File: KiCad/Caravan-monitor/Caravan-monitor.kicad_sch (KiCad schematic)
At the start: 11 parts, among them IC2 STM32L011F4P6TR, J1 Conn_ARM_JTAG_SWD_20, J2 PJ-059A, SW1 SW_SPST

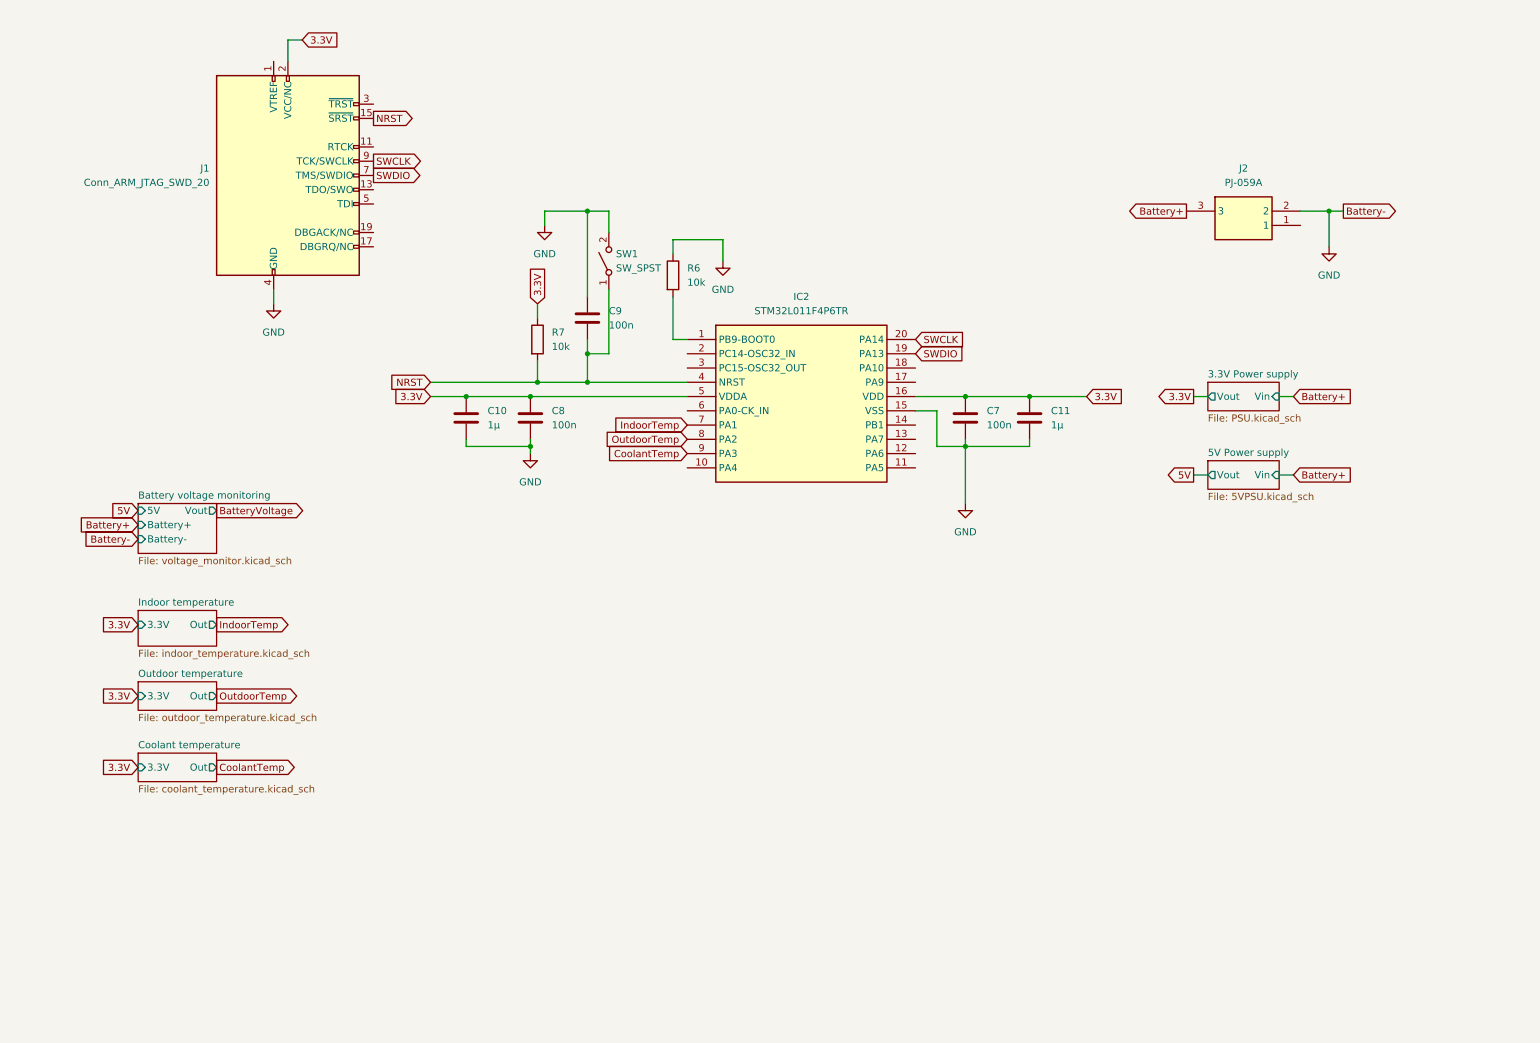
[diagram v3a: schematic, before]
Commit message: Display schematics
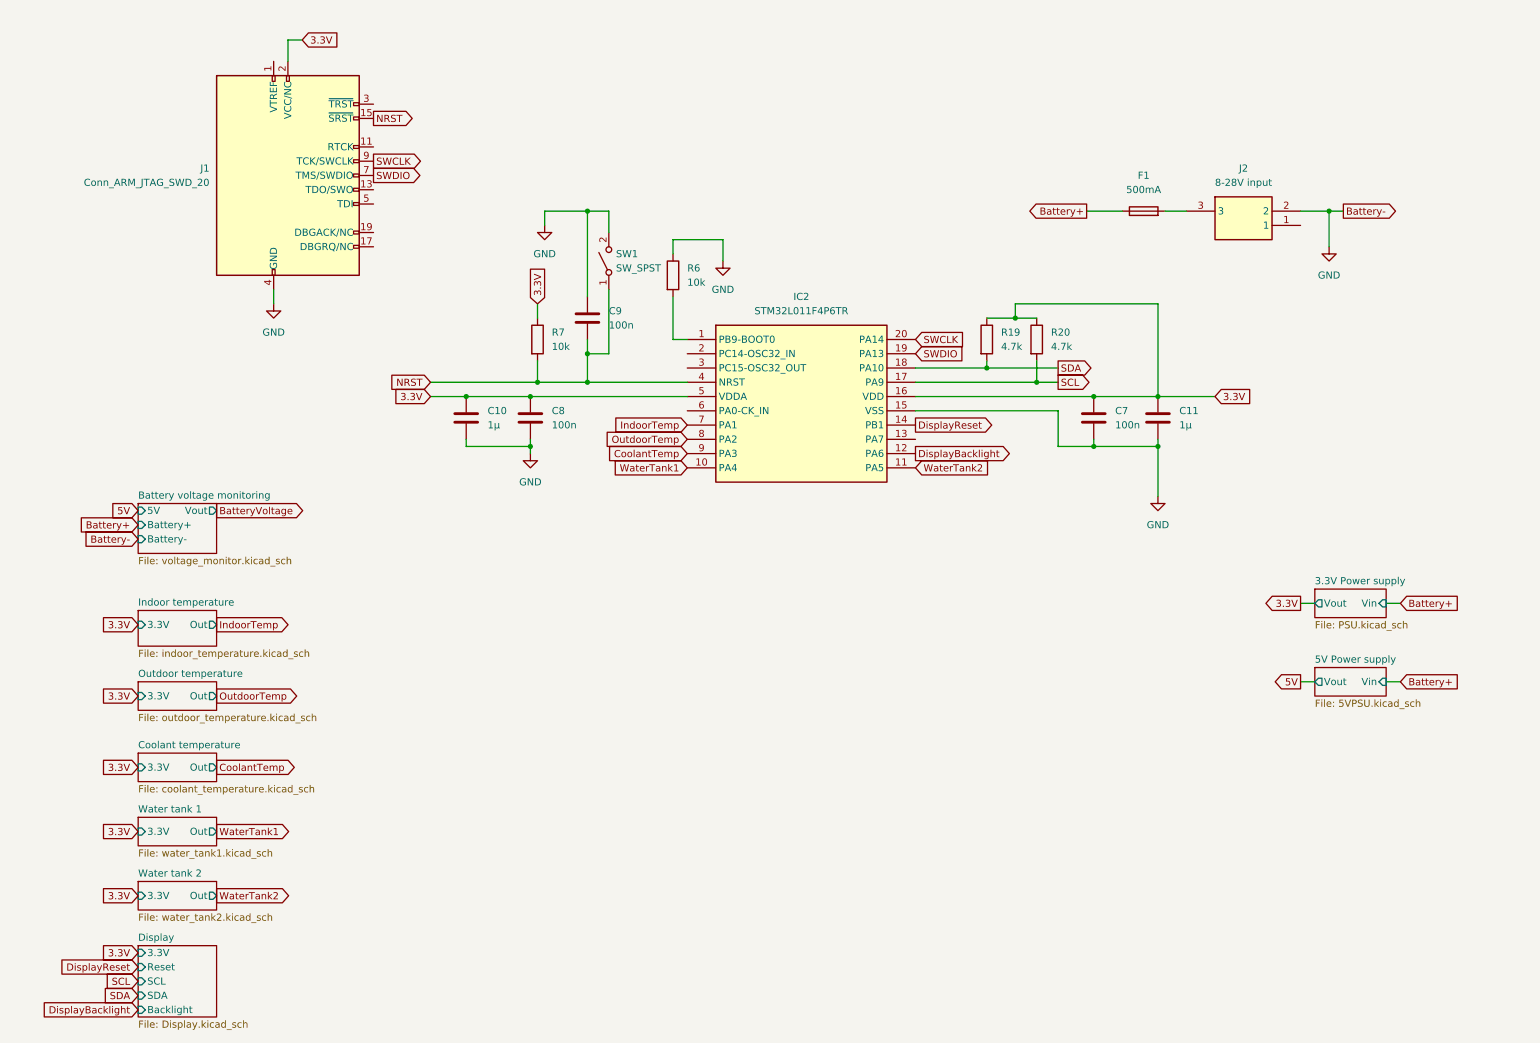
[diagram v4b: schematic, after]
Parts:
- added F1: 500mA, Fuse:Fuseholder_Clip-5x20mm_Littelfuse_111_Lateral_P18.80x5.00mm_D1.17mm_Horizontal, symbol Device:Fuse
- added R19, R20: 4.7k, Resistor_SMD:R_0805_2012Metric_Pad1.20x1.40mm_HandSolder, symbol Device:R
- J1: footprint Connector_IDC:IDC-Header_2x10_P2.54mm_Vertical -> Connector_IDC:IDC-Header_2x10_P2.54mm_Horizontal
- J2: value PJ-059A -> 8-28V input
- SW1: footprint (none) -> Button_Switch_SMD:SW_SPST_PTS645
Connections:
- net 3.3V: now also R19.1, R20.1
- net Battery+: now also F1.1; no longer J2.3
- net WaterTank1: now reaches IC2.10 (PA4)
- net WaterTank2: now reaches IC2.11 (PA5)
- net DisplayBacklight: now reaches IC2.12 (PA6)
- net DisplayReset: now reaches IC2.14 (PB1)
- net SCL: now reaches IC2.17 (PA9)
- net SCL: now also R20.2
- net SDA: now reaches IC2.18 (PA10)
- net SDA: now also R19.2
- new net: F1.2, J2.3
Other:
- added sheet Display (Display.kicad_sch)
- added sheet Water tank 1 (water_tank1.kicad_sch)
- added sheet Water tank 2 (water_tank2.kicad_sch)
- moved on the sheet: C11, C7

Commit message: Schematics done
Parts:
- removed IC2: STM32L011F4P6TR, SamacSys_Parts:SOP65P640X120-20N, symbol SamacSys_Parts:STM32L011F4P6TR
- added C25, C27, C28: 100n, Capacitor_SMD:C_0402_1005Metric_Pad0.74x0.62mm_HandSolder, symbol Device:C
- added C26: 1µ, Capacitor_SMD:C_0402_1005Metric_Pad0.74x0.62mm_HandSolder, symbol Device:C
- added C29, C30: 10p, Capacitor_SMD:C_0402_1005Metric_Pad0.74x0.62mm_HandSolder, symbol Device:C
- added D2: WT1_LED, LED_SMD:LED_0402_1005Metric_Pad0.77x0.64mm_HandSolder, symbol Device:LED
- added D3: WT2_LED, LED_SMD:LED_0402_1005Metric_Pad0.77x0.64mm_HandSolder, symbol Device:LED
- added FB1: 120R, Inductor_SMD:L_0402_1005Metric_Pad0.77x0.64mm_HandSolder, symbol Device:FerriteBead
- added J8: STM32 Pins, Connector_PinHeader_2.54mm:PinHeader_2x13_P2.54mm_Horizontal, symbol Connector_Generic:Conn_02x13_Counter_Clockwise
- added R23: 10k, Resistor_SMD:R_0402_1005Metric_Pad0.72x0.64mm_HandSolder, symbol Device:R
- added R25, R8: 1k, Resistor_SMD:R_0402_1005Metric_Pad0.72x0.64mm_HandSolder, symbol Device:R
- added SW2: SW_USER, Button_Switch_SMD:SW_SPST_PTS645, symbol Switch:SW_SPST
- added SW3: SW_DPDT_x2, Button_Switch_THT:SW_E-Switch_EG2219_DPDT_Angled, symbol Switch:SW_DPDT_x2
- added U2: STM32L010C6Tx, Package_QFP:LQFP-48_7x7mm_P0.5mm, symbol MCU_ST_STM32L0:STM32L010C6Tx
- added Y1: 16MHz, symbol Device:Crystal_GND24
- C10, C11, C7, C9: footprint Capacitor_SMD:C_0805_2012Metric_Pad1.18x1.45mm_HandSolder -> Capacitor_SMD:C_0402_1005Metric_Pad0.74x0.62mm_HandSolder
- C8: value 100n -> 10n; footprint Capacitor_SMD:C_0805_2012Metric_Pad1.18x1.45mm_HandSolder -> Capacitor_SMD:C_0402_1005Metric_Pad0.74x0.62mm_HandSolder
- R19, R20, R6, R7: footprint Resistor_SMD:R_0805_2012Metric_Pad1.20x1.40mm_HandSolder -> Resistor_SMD:R_0402_1005Metric_Pad0.72x0.64mm_HandSolder
- SW1: value SW_SPST -> SW_RESET
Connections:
- net BatteryVoltage: now also U2.46 (PB9)
- net CoolantTemp: now also U2.27 (PB14)
- net DisplayBacklight: now also U2.45 (PB8)
- net DisplayReset: now also U2.43 (PB7)
- net GND: now also C25.1, C26.2, C27.2, C28.2, C29.2, C30.2, J8.13 (Pin_13), R25.2, R8.2, SW2.1 (A), U2.23 (VSS), U2.35 (VSS), U2.47 (VSS), U2.8 (VSSA), Y1.2, Y1.4
- net IndoorTemp: now also U2.25 (PB12)
- net NRST: now also U2.7 (NRST)
- net OutdoorTemp: now also U2.26 (PB13)
- net SCL: now also R19.2, U2.30 (PA9); no longer R20.2
- net SDA: now also R20.2, U2.31 (PA10); no longer R19.2
- net SWCLK: now also U2.37 (PA14)
- net SWDIO: now also U2.34 (PA13)
- net WaterTank1: now also U2.28 (PB15)
- net WaterTank2: now also U2.21 (PB10)
- net BOOT0: now reaches R6.2
- net BOOT0: now also U2.44 (BOOT0)
- net 3.3V renamed +3.3V
- net +3.3V: now also C26.1, C27.1, C28.1, FB1.2, J8.26 (Pin_26), R23.1, U2.24 (VDD), U2.36 (VDD), U2.48 (VDD); no longer C10.1, C8.1
- net Battery+: no longer names the net of F1.1
- net Battery+: now also SW3.2 (B)
- new net: D2.2 (A), J8.1 (Pin_1), U2.10 (PA0)
- new net: J8.10 (Pin_10), U2.32 (PA11)
- new net: J8.11 (Pin_11), U2.33 (PA12)
- new net: J8.12 (Pin_12), U2.38 (PA15)
- new net: D3.2 (A), J8.2 (Pin_2), U2.11 (PA1)
- new net: J8.3 (Pin_3), U2.12 (PA2)
- new net: J8.4 (Pin_4), U2.13 (PA3)
- new net: J8.5 (Pin_5), U2.14 (PA4)
- new net: J8.6 (Pin_6), U2.15 (PA5)
- new net: J8.7 (Pin_7), U2.16 (PA6)
- new net: J8.8 (Pin_8), U2.17 (PA7)
- new net: J8.9 (Pin_9), U2.29 (PA8)
- new net: C25.2, R23.2, SW2.2 (B), U2.22 (PB11)
- new net: D3.1 (K), R8.1
- new net: D2.1 (K), R25.1
- new net +3.3VA: C10.1, C8.1, FB1.1, U2.9 (VDDA)
- new net +5V: J8.25 (Pin_25)
- new net +BATT: SW3.1 (A)
- new net OSC_IN: C30.1, U2.5 (PH0), Y1.1
- new net OSC_OUT: C29.1, U2.6 (PH1), Y1.3
- new net PB0: J8.20 (Pin_20), U2.18 (PB0)
- new net PB1: J8.19 (Pin_19), U2.19 (PB1)
- new net PB2: J8.18 (Pin_18), U2.20 (PB2)
- new net PB3: J8.17 (Pin_17), U2.39 (PB3)
- new net PB4: J8.16 (Pin_16), U2.40 (PB4)
- new net PB5: J8.15 (Pin_15), U2.41 (PB5)
- new net PB6: J8.14 (Pin_14), U2.42 (PB6)
- new net PC0: J8.24 (Pin_24), U2.1 (PC0)
- new net PC13: J8.23 (Pin_23), U2.2 (PC13)
- new net PC14: J8.22 (Pin_22), U2.3 (PC14)
- new net PC15: J8.21 (Pin_21), U2.4 (PC15)
- no-connect marks 0 -> 9
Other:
- note added: "Connector for the rest of the pins if more sensors are wanted"
- note added: "Power supply"
- note added: "ST-Link connector"
- moved on the sheet: C10, C11, C7, C8, F1, J1, J2, R19, R20, R7

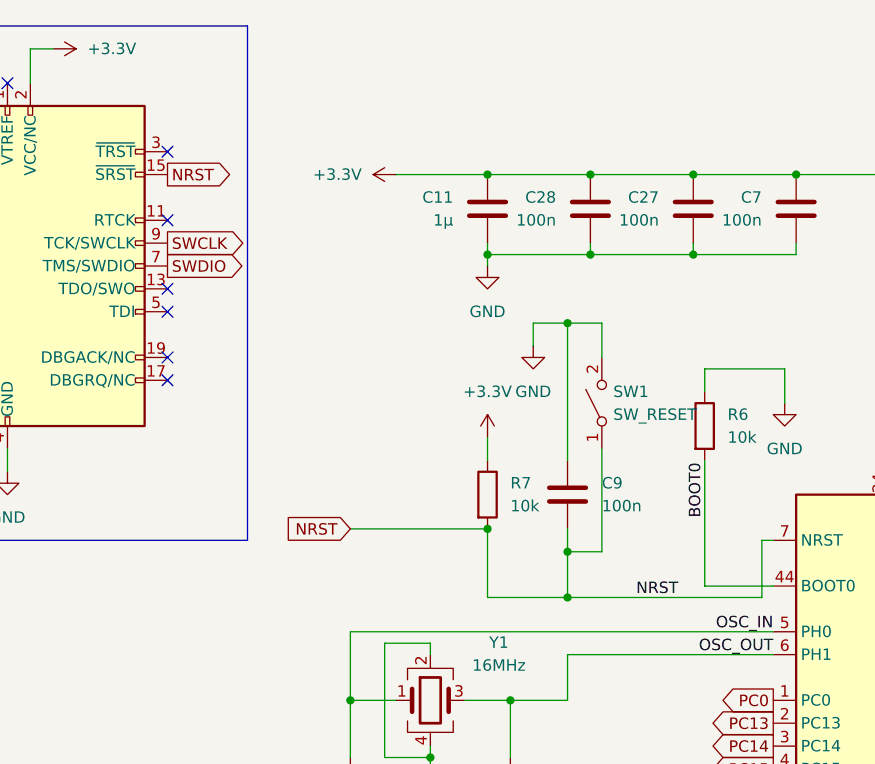
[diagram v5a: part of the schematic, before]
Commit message: 3.3V and 5V PSU layout done
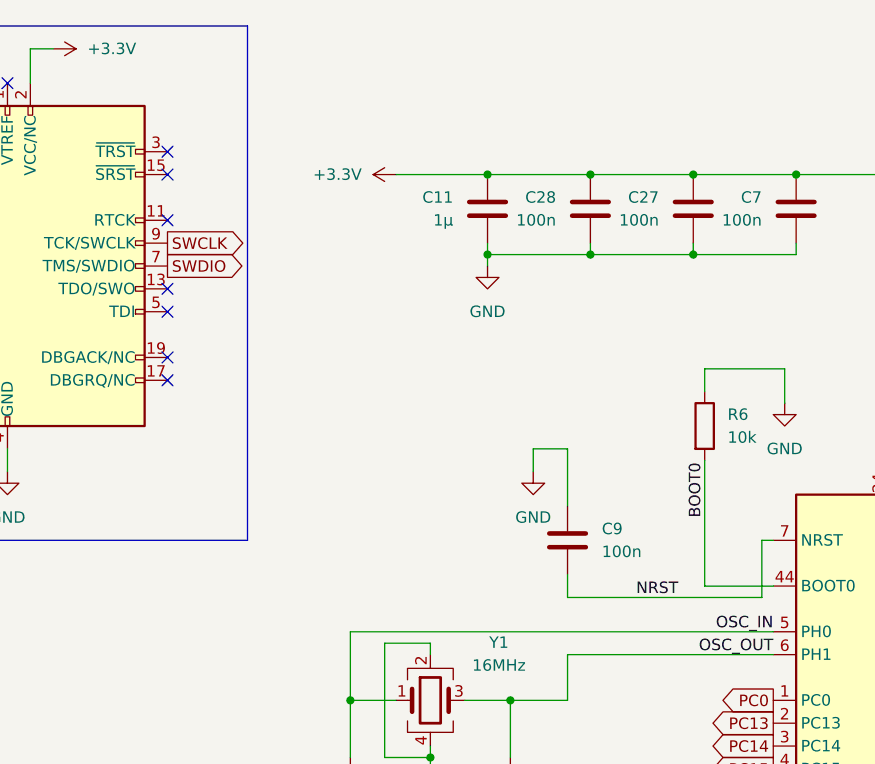
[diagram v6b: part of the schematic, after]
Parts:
- removed R7: 10k, Resistor_SMD:R_0402_1005Metric_Pad0.72x0.64mm_HandSolder, symbol Device:R
- removed SW1: SW_RESET, Button_Switch_SMD:SW_SPST_PTS645, symbol Switch:SW_SPST
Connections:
- net NRST: no longer J1.15 (~{SRST})
- no-connect marks 9 -> 10
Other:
- moved on the sheet: C9

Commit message: PCB Designed
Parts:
- removed J8: STM32 Pins, Connector_PinHeader_2.54mm:PinHeader_2x13_P2.54mm_Horizontal, symbol Connector_Generic:Conn_02x13_Counter_Clockwise
- Y1: footprint (none) -> Package_LGA:VLGA-4_2x2.5mm_P1.65mm
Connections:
- net PB0: no longer names the net of U2.18 (PB0)
- net PB1: no longer names the net of U2.19 (PB1)
- net PB2: no longer names the net of U2.20 (PB2)
- net PB3: no longer names the net of U2.39 (PB3)
- net PB4: no longer names the net of U2.40 (PB4)
- net PB5: no longer names the net of U2.41 (PB5)
- net PB6: no longer names the net of U2.42 (PB6)
- net PC0: no longer names the net of U2.1 (PC0)
- net PC13: no longer names the net of U2.2 (PC13)
- net PC14: no longer names the net of U2.3 (PC14)
- net PC15: no longer names the net of U2.4 (PC15)
- no-connect marks 10 -> 31
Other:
- removed sheet 5V Power supply
- sheet Battery voltage monitoring ports: added Vin; removed 5V
- moved on the sheet: R19, R20

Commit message: Version 0.1 complete
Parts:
- removed C29, C30: 10p, Capacitor_SMD:C_0402_1005Metric_Pad0.74x0.62mm_HandSolder, symbol Device:C
- removed Y1: 16MHz, Package_LGA:VLGA-4_2x2.5mm_P1.65mm, symbol Device:Crystal_GND24
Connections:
- net OSC_IN: no longer names the net of U2.5 (PH0)
- net OSC_OUT: no longer names the net of U2.6 (PH1)
- no-connect marks 31 -> 33
